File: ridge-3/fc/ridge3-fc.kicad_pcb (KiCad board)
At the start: 4 copper layers, 33.8 x 33.8 mm, 77 parts, among them Y1 8MHz

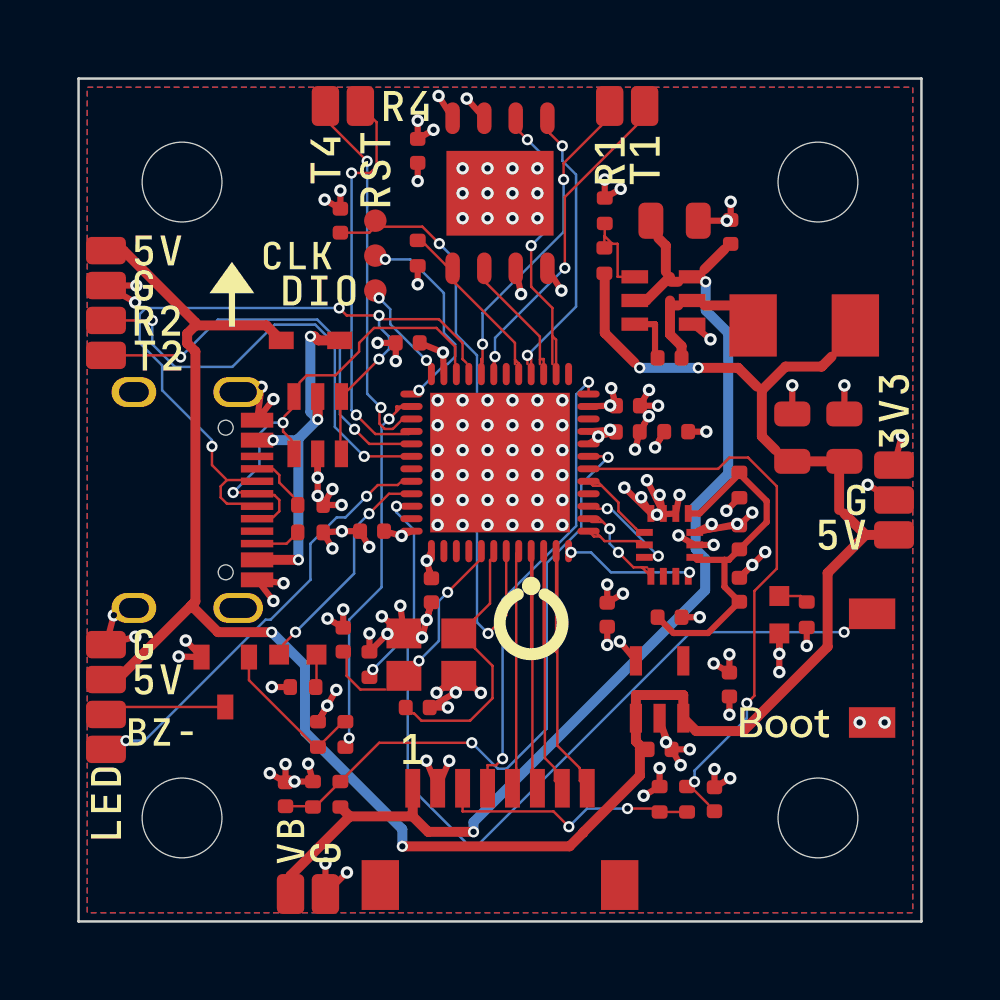
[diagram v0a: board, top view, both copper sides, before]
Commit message: Ridge 3 FC installed with outputs and panel; silkscreen keeps off the grommets
- FC: routed board (DRC 0/0/0), Gerbers, BOM/CPL, assembly PDF, 3x2 panel
  and renders under the ridge3-fc name; the old cheapdrone-fc files go
- Silkscreen placer: no ink under the soft-mount grommet flanges (the
  copper keep-out round each hole); marks can fit by outline; roomiest()
  finds the free spot with the largest clear circle
- ESC artwork: the OffGrid mark on top in the roomiest spot, the front
  arrow in its mirror spot; name and firmware centred when they fit; SWD
  labels placed before the motor numbers
- Panel check: 1 um tolerance for KiKit's re-segmented outline arcs
- ESC fanout: exposed-pad vias fall back to any clear spot in the pad
- verify: brand minimum mark size, no silk under grommets, ESC MCU bulk
- Docs: later ESC changes (no TVS, shared MCU bulk, neutral 30k/1k),
  SWD pad locations

Co-Authored-By: Claude Opus 5.5 <noreply@anthropic.com>
Claude-Session: https://claude.ai/code/session_01MaVFAzoExts7u2gmCraXFC
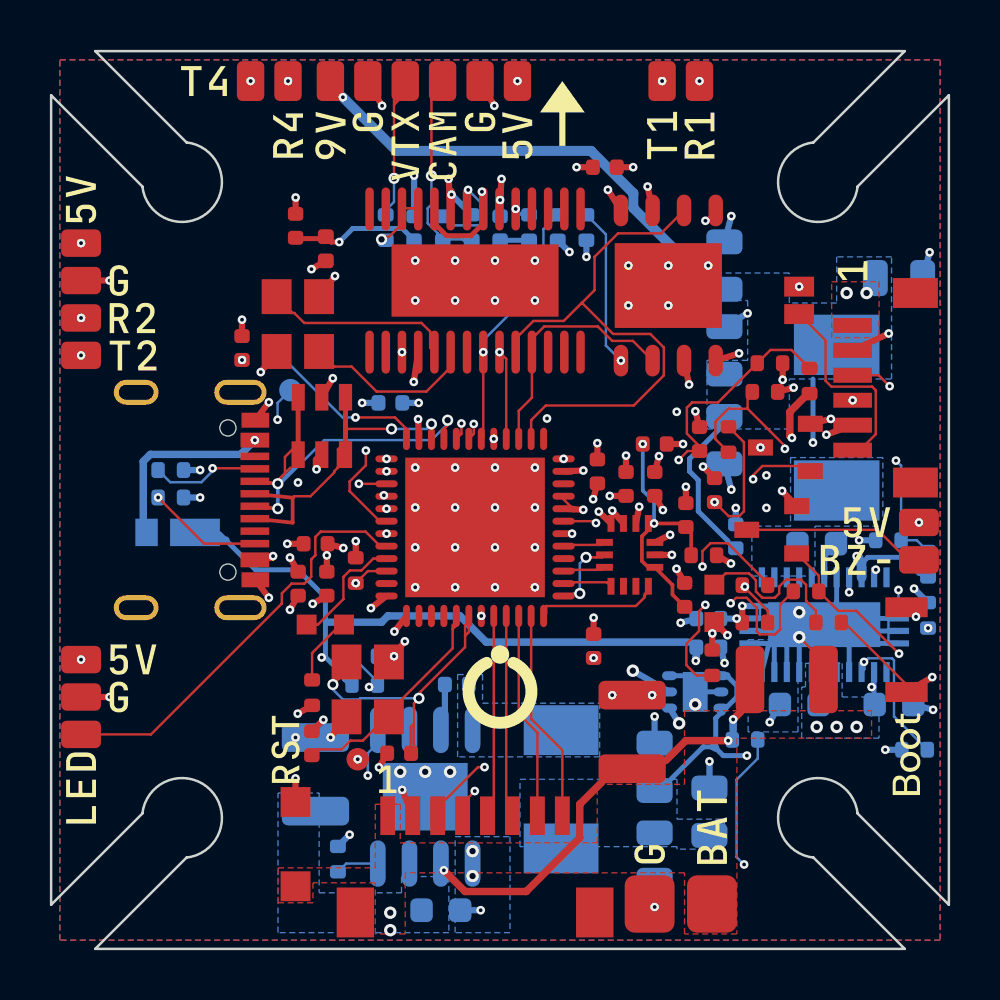
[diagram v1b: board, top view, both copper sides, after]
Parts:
- removed the D_USB at (92.4, 93.6)
- removed the J_USB at (87.8, 100.0)
- removed L1: 4.7uH, aio:IND-SMD_L5.4-W5.2_FXL0530
- removed the LED_PWR at (111.2, 104.6)
- removed the LED_STAT at (91.9, 106.2)
- removed P_3V3, P_G2, P_G3, P_VBAT: PAD_SIG, PAD_SIG
- removed the SW_BOOT at (114.9, 106.7)
- removed U_BUCK: LMR51420YDDCR, SOT-23-6_L2.9-W1.6-P0.95-LS2.9-BL
- removed the U_LDO at (106.4, 107.6)
- added C24: 100nF, C_0402_1005Metric, F.Cu at (91.9, 103.4)
- added C25: 100nF, C_0402_1005Metric, F.Cu at (105.1, 99.4)
- added C26: 1uF, C_0402_1005Metric, F.Cu at (106.2, 99.4)
- added C27: 4.7uF, C_0402_1005Metric, F.Cu at (92.6, 101.8)
- added C28: 100nF, C_0402_1005Metric, F.Cu at (103.8, 105.9)
- added C29: 12pF, C_0402_1005Metric, F.Cu at (92.5, 109.8)
- added C30: 12pF, C_0402_1005Metric, F.Cu at (96.0, 110.2)
- added C31: 4.7uF, C_0402_1005Metric, F.Cu at (107.5, 100.6)
- added C32: 100nF, C_0402_1005Metric, F.Cu at (107.4, 103.8)
- added C33: 100nF, C_0402_1005Metric, F.Cu at (106.2, 97.8)
- added C34: 100nF, C_0402_1005Metric, F.Cu at (104.2, 86.7)
- added C35: 4.7uF, C_0402_1005Metric, F.Cu at (91.8, 89.0)
- added C36: 100nF, C_0402_1005Metric, F.Cu at (89.7, 93.9)
- added C37: 100nF, C_0402_1005Metric, B.Cu at (100.0, 89.1)
- added C38: 100nF, C_0402_1005Metric, B.Cu at (96.6, 89.1)
- added C39: 100nF, C_0402_1005Metric, B.Cu at (97.7, 89.1)
- added D_TVS: SMF33A, SMF_L2.8-W1.8-LS3.7-RD, F.Cu at (91.8, 113.8)
- added D_USB: RB160VAM-40, SOD-323HE_L2.0-W1.4-LS2.5-RD, B.Cu at (86.8, 101.3)
- added FB_OSD: 600R@100MHz, L_0402_1005Metric, F.Cu at (93.0, 89.9)
- added J_HD: SH-6P V, CONN-SMD-6P-P1.00_BM06B-SRSS-TB-LF-SN, F.Cu at (115.4, 95.5)
- added J_USB: USB-C, USB-C-SMD_MC-311D, F.Cu at (87.8, 100.0)
- added LED_PWR: RED, LED0603-RD, F.Cu at (108.6, 104.1)
- added LED_STAT: BLUE, LED0603-RD, F.Cu at (93.0, 105.0)
- added L_5V: 4.7uH, IND-SMD_L5.4-W5.1_SPM5020T-100M-LR, B.Cu at (102.5, 111.6)
- added L_9V: 6.8uH, IND-SMD_L6.5-W6.5_VISHAY, B.Cu at (113.5, 96.7)
- added P_BAT: PAD_MOTOR, PAD_MOTOR, F.Cu at (108.5, 116.2)
- added P_BATG: PAD_MOTOR, PAD_MOTOR, F.Cu at (106.0, 116.2)
- added P_CAM: PAD_SIG, PAD_SIG, F.Cu at (97.7, 83.2)
- added P_CAM5V: PAD_SIG, PAD_SIG, F.Cu at (100.7, 83.2)
- added P_CAMG: PAD_SIG, PAD_SIG, F.Cu at (99.2, 83.2)
- added P_VTX: PAD_SIG, PAD_SIG, F.Cu at (96.2, 83.2)
- added P_VTX9V: PAD_SIG, PAD_SIG, F.Cu at (93.2, 83.2)
- added P_VTXG: PAD_SIG, PAD_SIG, F.Cu at (94.7, 83.2)
- added Q_VTX: AO3400A, SOT-23-3_L2.9-W1.3-P1.90-LS2.4-BR, F.Cu at (111.4, 97.9)
- added R16: 10R, R_0402_1005Metric, F.Cu at (108.2, 102.2)
- added R17: 10k, R_0402_1005Metric, B.Cu at (103.5, 89.1)
- added R18: 10k, R_0402_1005Metric, B.Cu at (101.2, 89.1)
- added R19: 10k, R_0402_1005Metric, B.Cu at (102.3, 89.1)
- added R20: 75R, R_0402_1005Metric, B.Cu at (98.9, 89.1)
- added R21: 75R, R_0402_1005Metric, B.Cu at (95.4, 89.1)
- added R22: 5.1k, R_0402_1005Metric, B.Cu at (86.8, 98.8)
- added R23: 5.1k, R_0402_1005Metric, B.Cu at (86.8, 99.9)
- added R24: 1k, R_0402_1005Metric, F.Cu at (113.2, 104.9)
- added R25: 330R, R_0402_1005Metric, F.Cu at (92.5, 107.7)
- added R26: 100R, R_0402_1005Metric, F.Cu at (112.3, 103.7)
- added R27: 10k, R_0402_1005Metric, F.Cu at (108.5, 106.5)
- added SJ_SBUS: SJ_OPEN, SJ_OPEN, F.Cu at (112.0, 92.0)
- added SW_BOOT: BOOT, KEY-SMD_B3U-1000PM, F.Cu at (116.3, 106.0)
- added U_BUCK5: LMR38020F, ESOP-8_L4.9-W3.9-P1.27-LS6.0-BL-EP-1, B.Cu at (97.0, 111.9)
- added U_BUCK9: LM76003, WQFN-30_L6.0-W4.0-P0.50-BL-EP, B.Cu at (113.0, 105.0)
- added U_LDO: TLV76733 3.3V, WSON-6_L2.0-W2.0-P0.65-TL-EP, B.Cu at (107.8, 107.7)
- added U_OSD: AT7456E, TSSOP-28_L9.7-W4.4-P0.65-LS6.4-BL-EP-2, F.Cu at (99.0, 91.2)
- added Y2: 27MHz, CRYSTAL-SMD_4P-L3.2-W2.5-BL, F.Cu at (91.9, 92.9)
- C1, C10: value 100nF -> 10uF; footprint C_0402_1005Metric -> C_1210_3225Metric
- C11, C5: footprint C_0402_1005Metric -> C_0603_1608Metric; moved to B.Cu
- C12: value 100nF -> 470nF; footprint C_0402_1005Metric -> C_0603_1608Metric; moved to B.Cu
- C13: value 100nF -> 2.2uF; footprint C_0402_1005Metric -> C_0603_1608Metric; moved to B.Cu
- C14: value 100nF -> 1uF; moved to B.Cu
- C15, C8: value 1uF -> 22uF; footprint C_0402_1005Metric -> C_0805_2012Metric; moved to B.Cu
- C16, C9: value 4.7uF -> 22uF; footprint C_0402_1005Metric -> C_0805_2012Metric; moved to B.Cu
- C17: value 100nF -> 22uF; footprint C_0402_1005Metric -> C_0805_2012Metric; moved to B.Cu
- C18: value 12pF -> 22uF; footprint C_0402_1005Metric -> C_0805_2012Metric; moved to B.Cu
- C19: value 12pF -> 1uF; moved to B.Cu
- C20, C23, C7, TP_SWCLK, TP_SWDIO: moved to B.Cu
- C3: value 10uF -> 100nF; footprint C_0805_2012Metric -> C_0402_1005Metric
- C4: value 100nF -> 10uF; footprint C_0402_1005Metric -> C_1210_3225Metric; moved to B.Cu
- C6: value 22uF -> 100nF; footprint C_0805_2012Metric -> C_0402_1005Metric; moved to B.Cu
- H1, H2, H3, H4: footprint HOLE_M3 -> MOUNT_M2_SLOT
- Q_BZ: value 2N7002 -> AO3400A
- R10: value 5.1k -> 24.9k; moved to B.Cu
- R11: value 5.1k -> 100R
- R12: value 1k -> 100k
- R13: value 1k -> 100k; moved to B.Cu
- R14: value 100R -> 12.4k; moved to B.Cu
- R3: value 10k -> 30k
- R4: value 1k -> 2k
- R5: value 15k -> 25.5k; moved to B.Cu
- R6: value 2k -> 100k; moved to B.Cu
- R7: value 10k -> 24.9k; moved to B.Cu
- R8: value 10R -> 24.3k; moved to B.Cu
- R9: value 10k -> 100k; moved to B.Cu
- U_FLASH: value W25Q128JVPIQ -> W25Q128JVPIM
- U_IMU: value ICM-42688-P -> BMI270
- moved P_BZ+ 33.2 mm to (116.8, 100.9)
- moved P_BZ- 33.2 mm to (116.8, 102.4)
- moved P_5V 33.0 mm to (83.2, 106.4)
- moved C4 27.4 mm to (92.6, 111.0)
- moved C18 26.6 mm to (116.0, 91.1), turned to 0 degrees
- moved R5 26.3 mm to (93.5, 114.4)
- moved R10 26.1 mm to (116.6, 110.0), turned to 180 degrees
- moved R13 25.5 mm to (117.2, 102.6), turned to 90 degrees
- moved R4 25.2 mm to (110.8, 94.5), turned to 0 degrees
- moved R3 25.1 mm to (112.4, 95.2)
- moved C5 24.0 mm to (97.6, 116.5)
- moved R9 23.5 mm to (109.8, 109.6), turned to 0 degrees
- moved R14 23.1 mm to (115.6, 101.6), turned to 180 degrees
- moved Q_BZ 22.7 mm to (110.9, 101.2), turned to 0 degrees
- moved C13 22.1 mm to (115.8, 108.2), turned to 0 degrees
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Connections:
- C1 pad 1: ADC_CURR -> VBAT
- C10 pad 1: +3V3 -> VBAT
- C11 pad 1: +3V3 -> VBAT
- C12 pad 1: +3V3 -> BUCK9_CB
- C12 pad 2: GND -> BUCK9_SW
- C13 pad 1: +3V3 -> BUCK9_VCC
- C14 pad 1: +3V3 -> +9V
- C15 pad 1: +3V3 -> +9V
- C16 pad 1: +3V3 -> +9V
- C17 pad 1: NRST -> +9V
- C18 pad 1: HSE_IN -> +9V
- C19 pad 1: HSE_OUT -> +5V
- C2 pad 1: ADC_VBAT -> ADC_CURR
- C20 pad 1: +3V3_GYRO -> +3V3
- C21 pad 1: +3V3_GYRO -> +3V3
- C22 pad 1: +3V3_GYRO -> +3V3
- C3 pad 1: VBAT -> ADC_VBAT
- C5 pad 1: BUCK_CB -> VBAT
- C5 pad 2: BUCK_SW -> GND
- C6 pad 1: +5V -> BUCK5_CB
- C6 pad 2: GND -> BUCK5_SW
- C9 pad 1: +3V3 -> +5V
- R10 pad 1: USB_CC1 -> BUCK9_EN
- R11 pad 1: USB_CC2 -> VTX_OFF
- R11 pad 2: GND -> VTX_OFF_G
- R12 pad 1: +3V3 -> VTX_OFF_G
- R12 pad 2: LED_PWR_A -> GND
- R13 pad 1: +3V3 -> +9V
- R13 pad 2: LED0_A -> BUCK9_FB
- R14 pad 1: BEEPER -> BUCK9_FB
- R14 pad 2: BEEPER_G -> GND
- R15 pad 1: BEEPER_G -> BOOT0
- R5 pad 1: +5V -> BUCK5_RT
- R5 pad 2: BUCK_FB -> GND
- R6 pad 1: BUCK_FB -> +5V
- R6 pad 2: GND -> BUCK5_FB
- R7 pad 1: BOOT0 -> BUCK5_FB
- R8 pad 1: +3V3 -> BUCK9_RT
- R8 pad 2: +3V3_GYRO -> GND
- R9 pad 1: +3V3 -> VBAT
- R9 pad 2: FLASH_CS -> BUCK9_EN
- U_FC pad 30: (no net) -> OSD_CS
- U_FC pad 43: (no net) -> VTX_OFF
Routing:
- net BUCK9_EN: track 0.00 -> 36.1 mm, vias 0 -> 3
- net +9V: track 0.00 -> 35.9 mm, vias 0 -> 5
- net +3V3_OSD: track 0.00 -> 33.8 mm, vias 0 -> 4
- net CUR: track 10.5 -> 32.6 mm
- net UART1_TX: track 13.4 -> 33.4 mm, vias 2 -> 4
- net UART2_RX: track 18.4 -> 37.8 mm, vias 2 -> 3
- net UART1_RX: track 13.0 -> 32.2 mm, vias 2 -> 3
- net +5V: track 88.2 -> 105.9 mm, vias 4 -> 10
- net VTX_OFF: track 0.00 -> 17.3 mm, vias 0 -> 2
- net VBAT: track 42.6 -> 27.2 mm, vias 2 -> 9
- net BEEPER_G: track 6.33 -> 19.0 mm, vias 0 -> 2
- net USB_DM: track 29.7 -> 17.2 mm, vias 4 -> 3
- net NRST: track 24.6 -> 13.0 mm, vias 2 -> 3
- net BEEPER: track 15.3 -> 26.7 mm
- net BOOT0: track 35.9 -> 25.2 mm, vias 3 -> 2
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- added copper zone on In4.Cu, net +3V3
- added copper zone on B.Cu, net +5V
- added copper zone on B.Cu, net +9V
- added copper zone on F.Cu, net +9V
- added copper zone on B.Cu, net BUCK5_SW
- added copper zone on B.Cu, net BUCK9_SW
- added copper zone on B.Cu, net VBAT
- added copper zone on F.Cu, net VBAT
- removed copper zone on In2.Cu, net +3V3
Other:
- board size 33.8 x 33.8 mm -> 36 x 36 mm
- copper layers 4 -> 6

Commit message: FC: rerouted with the USB-C at the edge; outputs, panel and renders
make.py --reroute result (seed 0): DRC 0 errors, 0 warnings, 0
unconnected; copper nets match circuit.py; BOM/CPL and the 3 x 2 panel
regenerated.

Co-Authored-By: Claude Opus 5.5 <noreply@anthropic.com>
Claude-Session: https://claude.ai/code/session_01MaVFAzoExts7u2gmCraXFC
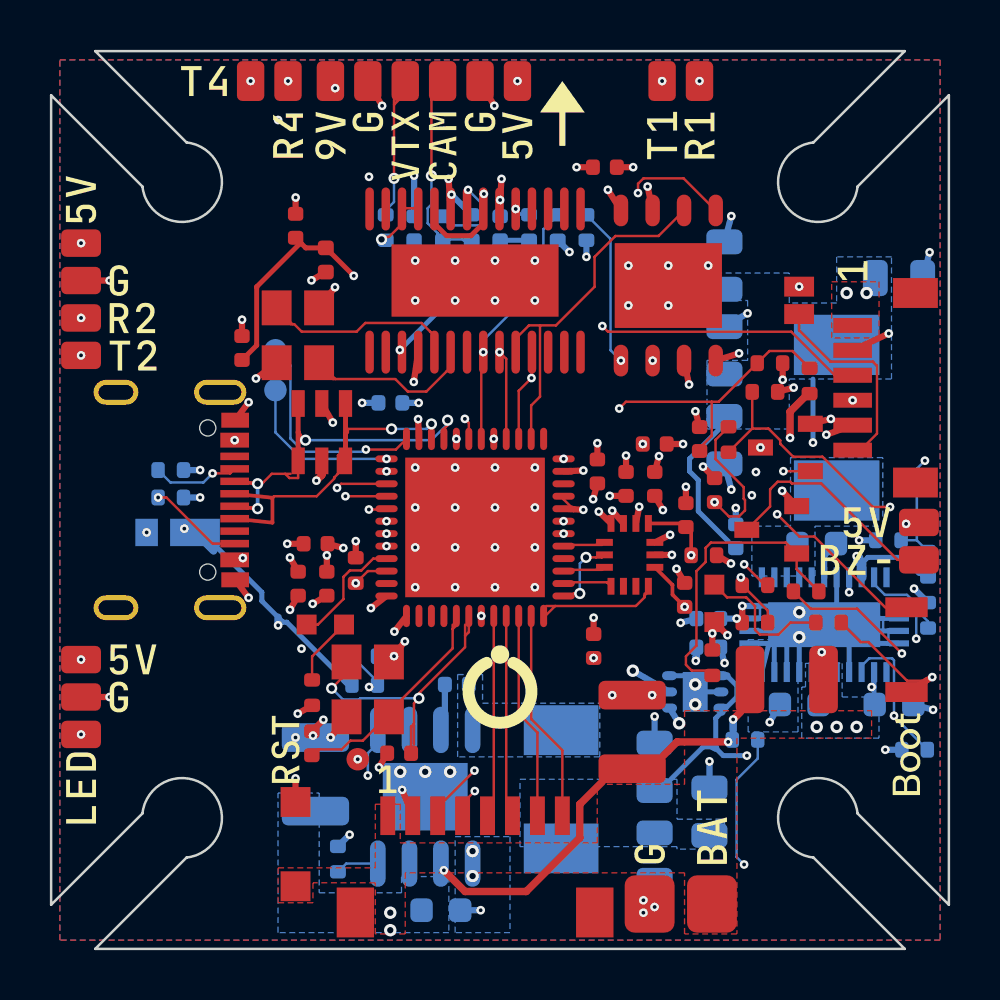
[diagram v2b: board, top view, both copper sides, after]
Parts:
- moved J_USB 0.81 mm to (87.0, 100.0)
- moved TP_SWCLK 0.60 mm to (91.0, 95.6)
- moved FB_OSD 0.45 mm to (93.0, 90.4)
- moved Y2 0.45 mm to (91.9, 93.4)
- moved U_ESD 0.25 mm to (92.9, 97.3)
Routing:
- net +5V: track 105.9 -> 95.9 mm
- net +9V: track 35.9 -> 43.3 mm, vias 5 -> 6
- net BEEPER: track 26.7 -> 34.1 mm
- net SPI2_SCK: track 22.2 -> 14.8 mm
- net BEEPER_G: track 19.0 -> 12.1 mm, vias 2 -> 0
- net UART1_TX: track 33.4 -> 29.7 mm, vias 4 -> 3
- net BUCK9_FB: track 10.4 -> 13.6 mm
- net CUR: track 32.6 -> 35.5 mm
- net VTX_OFF: track 17.3 -> 20.0 mm, vias 2 -> 3
- net BZ-: track 7.40 -> 9.40 mm
- net SWDIO: track 6.96 -> 8.88 mm
- net SPI2_MOSI: track 14.6 -> 16.5 mm
- net +3V3_GYRO: track 10.5 -> 12.3 mm, vias 2 -> 3
- net USB_DM: track 17.2 -> 15.4 mm, vias 3 -> 4
- net USB_VBUS: track 15.4 -> 13.8 mm
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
